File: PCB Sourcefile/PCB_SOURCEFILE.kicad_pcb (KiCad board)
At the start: 2 copper layers, 120 x 100 mm, 15 parts, among them J1 Conn_01x04, J2 Conn_01x08, J3 Conn_01x06, J4 Conn_01x04

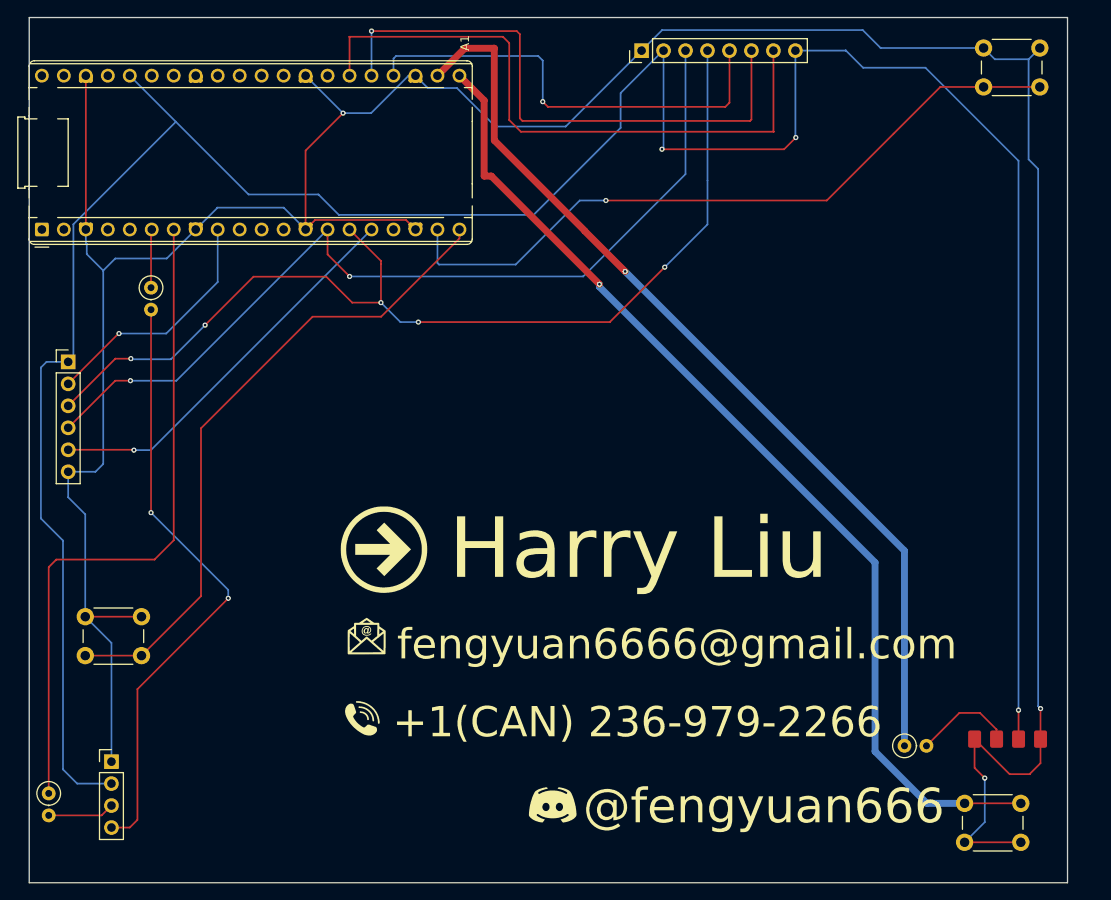
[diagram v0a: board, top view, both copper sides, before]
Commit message: Make PCB 100mmx100mm
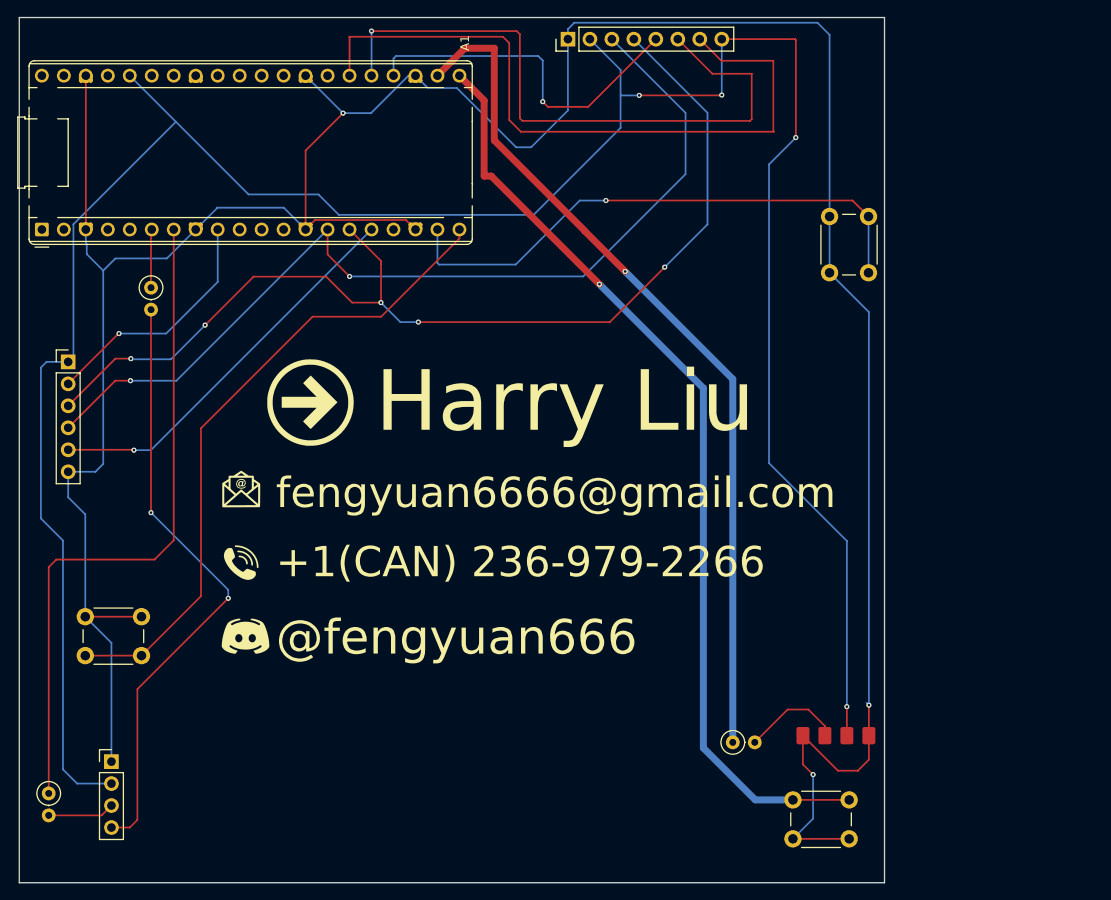
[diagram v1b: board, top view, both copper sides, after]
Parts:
- moved G*** 40.5 mm to (175.0, 121.5)
- moved OLEDscreenbutton1 31.5 mm to (242.5, 79.5), turned to 90 degrees
- moved G*** 22.8 mm to (174.5, 113.0)
- moved G*** 22.3 mm to (174.5, 104.5)
- moved LED_Buttons1 19.8 mm to (238.3, 140.4)
- moved 330Ohms1 19.8 mm to (231.3, 133.8)
- moved J4 19.8 mm to (239.4, 133.0)
- moved G*** 19.0 mm to (182.5, 94.5)
- moved J2 8.61 mm to (212.3, 52.5)
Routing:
- net Net-(A1-3V3): track 304.2 -> 281.6 mm, vias 3 -> 4
- net Net-(A1-GPIO14): track 82.1 -> 64.1 mm
- net Net-(J1-Pin_1): track 357.6 -> 343.9 mm
- net Net-(A1-GPIO18): track 52.4 -> 40.9 mm
- net Net-(A1-GPIO17): track 108.1 -> 99.5 mm
- net Net-(A1-GPIO16): track 117.9 -> 109.3 mm
- net Net-(A1-GPIO20): track 72.7 -> 81.1 mm
- net Net-(A1-GPIO19): track 67.1 -> 74.6 mm
- net Net-(A1-GPIO11): track 117.0 -> 121.9 mm
- net Net-(A1-GPIO10): track 104.0 -> 108.8 mm
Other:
- board size 120 x 100 mm -> 100 x 100 mm
